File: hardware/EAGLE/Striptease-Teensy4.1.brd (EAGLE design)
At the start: 48.3 x 114.3 mm, 18 parts, among them IC1 74245N

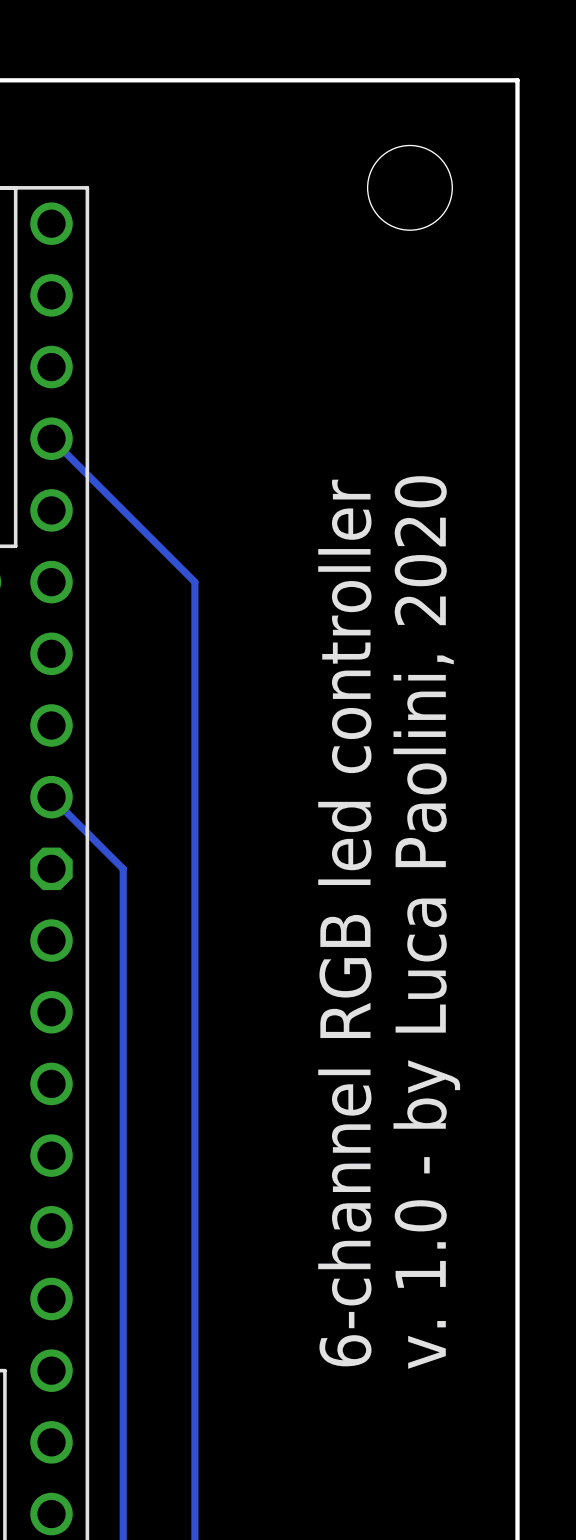
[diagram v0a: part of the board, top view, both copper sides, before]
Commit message: Fix circuit for Teensy 4.1.
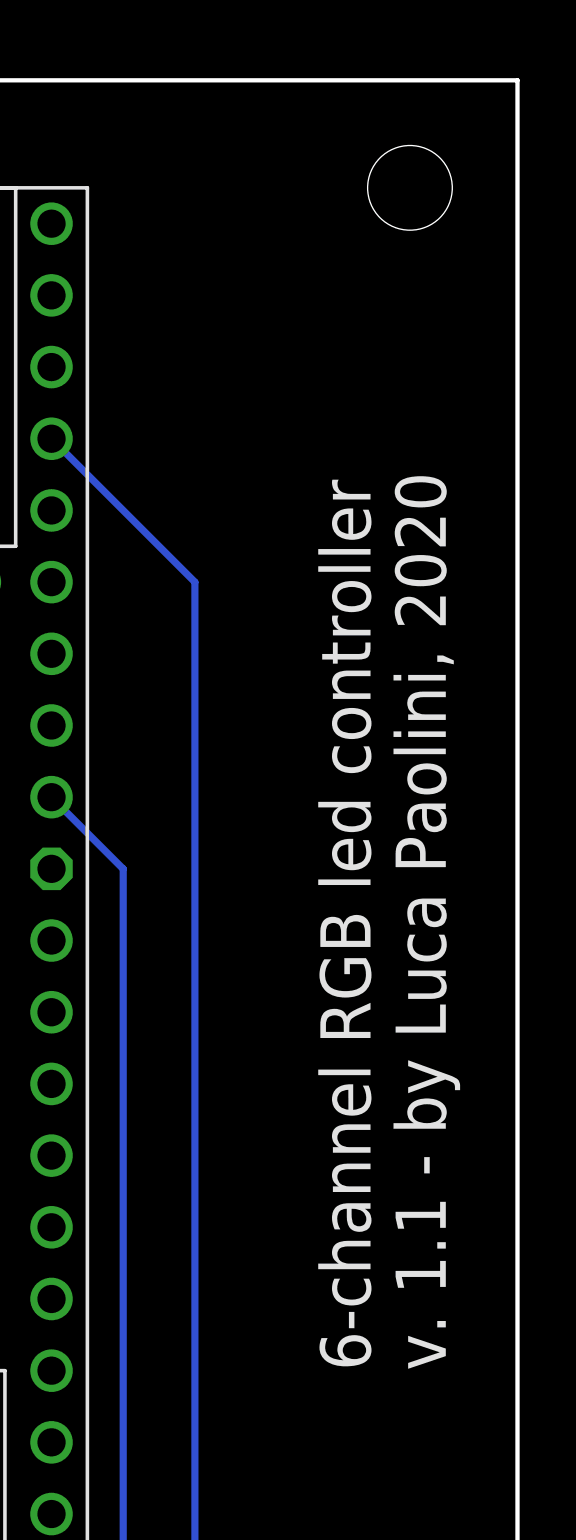
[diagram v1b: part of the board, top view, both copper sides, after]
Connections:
- removed net N$4: C2.2, C3.2, IC1.19
- net GND: now also C2.2, C3.2, IC1.19, U$3.GND2
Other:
- board text added: "6-channel RGB led controller v. 1.1 - by Luca Paolini, 2020"
- board text removed: "6-channel RGB led controller v. 1.0 - by Luca Paolini, 2020"
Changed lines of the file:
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@@
 <wire x1="3.81" y1="-3.81" x2="3.81" y2="110.49" width="0.1524" layer="20"/>
 <text x="49.53" y="64.77" size="1.778" layer="25" font="vector" rot="R90">6-channel RGB led controller
-v. 1.0 - by Luca Paolini, 2020</text>
+v. 1.1 - by Luca Paolini, 2020</text>
 </plain>
 <attributes>
@@
 <signal name="GND">
 <contactref element="IC1" pad="10"/>
+<contactref element="J1" pad="2"/>
+<contactref element="J2" pad="3"/>
+<contactref element="J3" pad="2"/>
+<contactref element="C2" pad="2"/>
+<contactref element="IC1" pad="19"/>
+<contactref element="C3" pad="2"/>
+<contactref element="C1" pad="2"/>
 <contactref element="IC1" pad="2"/>
 <contactref element="IC1" pad="5"/>
-<contactref element="C1" pad="2"/>
-<contactref element="U$3" pad="GND6"/>
 <contactref element="U$3" pad="GND1"/>
-<contactref element="U$3" pad="GND3"/>
 <polygon width="0.1524" layer="16">
 <vertex x="3.81" y="110.49"/>
@@
 <vertex x="3.81" y="-3.81"/>
 </polygon>
-<polygon width="0.254" layer="1">
+<polygon width="0.1524" layer="1">
 <vertex x="3.81" y="110.49"/>
 <vertex x="52.07" y="110.49"/>
@@
 <vertex x="3.81" y="-3.81"/>
 </polygon>
-<contactref element="J1" pad="2"/>
-<contactref element="J2" pad="3"/>
-<contactref element="J3" pad="2"/>
+<contactref element="U$3" pad="GND2"/>
+<contactref element="U$3" pad="GND3"/>
+<contactref element="U$3" pad="GND6"/>
 </signal>
 <signal name="N$6">
@@
 <wire x1="20.32" y1="2.54" x2="19.05" y2="3.81" width="0.254" layer="16"/>
 </signal>
-<signal name="N$4">
-<contactref element="C2" pad="2"/>
-<contactref element="IC1" pad="19"/>
-<contactref element="C3" pad="2"/>
-<wire x1="38.1" y1="31.75" x2="45.72" y2="31.75" width="0" layer="19" extent="1-1"/>
-<wire x1="12.7" y1="19.05" x2="38.1" y2="31.75" width="0" layer="19" extent="1-1"/>
-</signal>
 </signals>
